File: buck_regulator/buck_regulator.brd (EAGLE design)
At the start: 69.5 x 52.1 mm, 12 parts

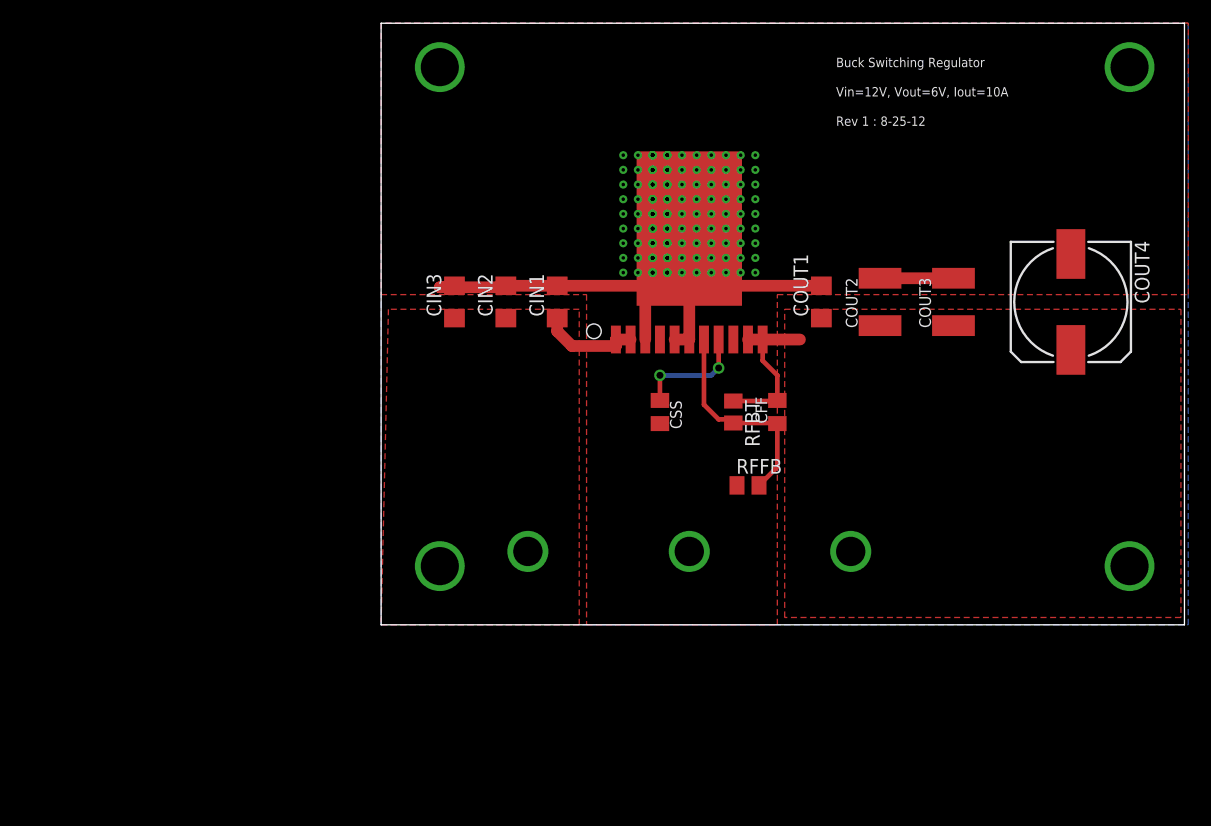
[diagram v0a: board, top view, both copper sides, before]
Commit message: buck_regulator: re-route for revision B
Change-Id: Ie95bbfd6e64e4db471db740f6a7ad1b08f6b97fa
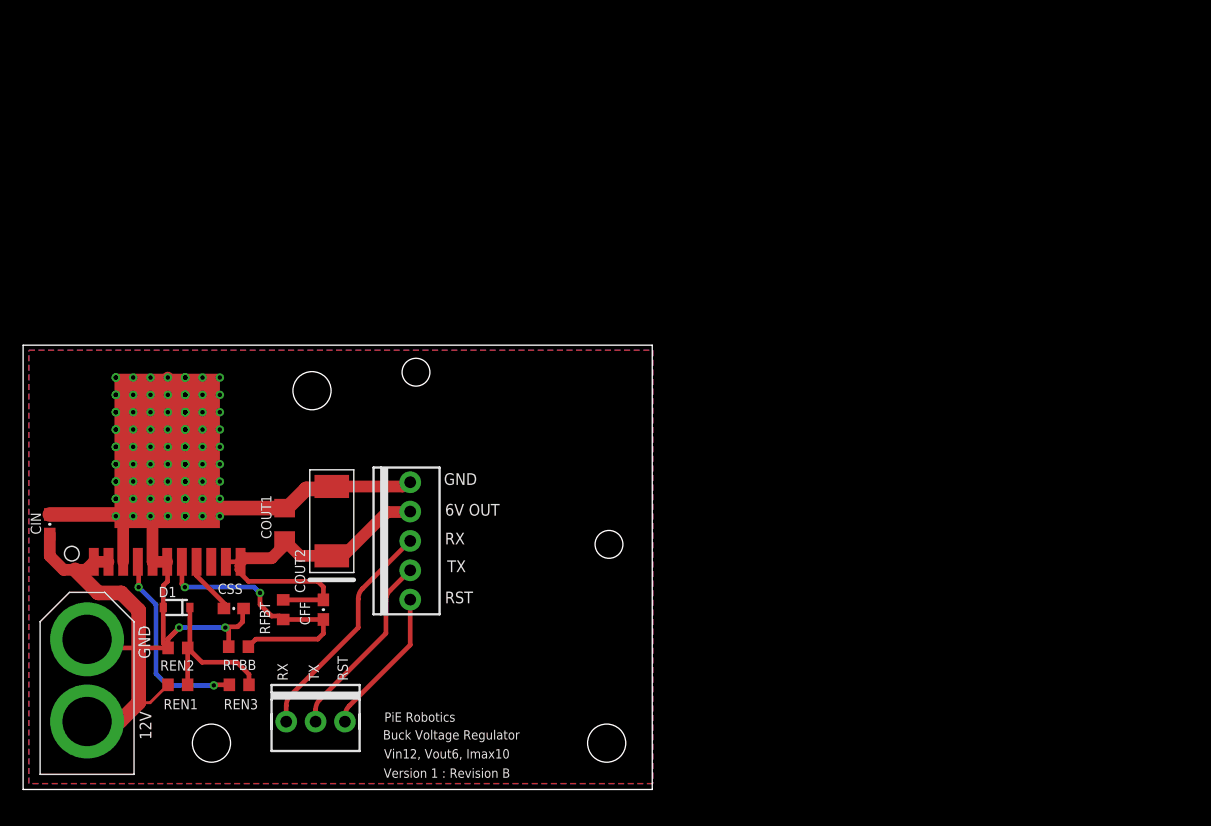
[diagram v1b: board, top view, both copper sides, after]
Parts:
- removed CIN1, CIN2, CIN3: (no value), resistor:C1206
- removed COUT3: (no value), resistor:C1812K
- removed COUT4: (no value), resistor:153CLV-1014
- removed RFFB: 2.37k, resistor:M0805
- added CIN: 10uF, pie:0603-CAP
- added D1: 5.1V, SparkFun:SOD-323
- added JP1: (no value), pie:1X03
- added REN1: 60k, pie:R0603
- added REN2: 30k, pie:R0603
- added REN3: 100, pie:R0603
- added RFBB: 2.37k, pie:R0603
- added U$2: XT60CONNECTOR, pie:XT60CONNECTOR
- added U$3, U$4, U$5: (no value), SparkFun:STAND-OFF
- added U$6, U$7: (no value), stand_off_servoc:STAND_OFF_SERVOC
- added U$8: M05, pie:1X05-MTA
- CFF: device resistor:C0805K -> pie:0603-CAP
- COUT1: value (none) -> 47uF; device resistor:C1206 -> SparkFun:1206
- COUT2: value (none) -> 470uF; device resistor:C1812K -> TANT_CASE_E:TANT_CASE_E
- CSS: value .47u -> .47uF; device resistor:C0805K -> pie:0603-CAP
- RFBT: device resistor:M0805 -> pie:R0603
- moved COUT2 51.1 mm to (26.2, 24.2)
- moved COUT1 50.3 mm to (22.1, 23.9)
- moved U$1 49.1 mm to (12.0, 30.3)
- moved CFF 42.8 mm to (25.5, 16.6), turned to 270 degrees
- moved RFBT 42.5 mm to (22.0, 16.6), turned to 90 degrees
- moved CSS 40.6 mm to (17.7, 16.6), turned to 0 degrees
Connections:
- removed net EN: U$1.4
- new net N$1: REN3.2, U$1.4
- new net N$2: JP1.1, U$8.3
- new net N$3: D1.1, REN1.1, REN2.2, REN3.1
- new net N$4: JP1.2, U$8.2
- new net N$5: JP1.3, U$8.1
- net FB: now also CFF.2, RFBB.1, RFBT.1; no longer CFF.1, RFBT.2, RFFB.2
- net GND: now also CIN.2, COUT2.NEG, D1.2, REN2.1, RFBB.2, U$2.GND, U$8.5; no longer CIN1.2, CIN2.2, CIN3.2, COUT2.2, COUT3.2, COUT4.-, RFFB.1
- net VIN: now also CIN.1, REN1.2, U$2.12V; no longer CIN1.1, CIN2.1, CIN3.1
- net VOUT: now also CFF.1, COUT2.POS, RFBT.2, U$8.4; no longer CFF.2, COUT2.1, COUT3.1, COUT4.+, RFBT.1
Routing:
- net GND: track 43.5 -> 72.4 mm, vias 153 -> 91
- net VIN: track 8.57 -> 31.0 mm
- net N$2: track 0.00 -> 19.9 mm, vias 1 -> 0
- net VOUT: track 14.1 -> 32.6 mm
- net N$1: track 0.00 -> 17.1 mm, vias 1 -> 2
- net N$4: track 0.00 -> 16.3 mm, vias 1 -> 0
- net N$3: track 0.00 -> 13.9 mm
- net N$5: track 0.00 -> 12.8 mm, vias 1 -> 0
- net FB: track 18.7 -> 24.2 mm, vias 0 -> 2
- net SS: track 9.98 -> 5.12 mm, vias 2 -> 0
- added copper zone on layer 1, net N$21
- removed copper zone on layer 1, net GND
- removed copper zone on layer 1, net VIN
- removed copper zone on layer 1, net VOUT
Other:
- board size 69.5 x 52.1 mm -> 54.4 x 38.4 mm
- board text added: "12V"
- board text added: "6V OUT"
- board text added: "Buck Voltage Regulator"
- board text added: "GND"
- board text added: "PiE Robotics"
- board text added: "RST"
- board text added: "RX"
- board text added: "TX"
- board text added: "Version 1 : Revision B"
- board text added: "Vin12, Vout6, Imax10"
- board text removed: "Buck Switching Regulator"
- board text removed: "Rev 1 : 8-25-12"
- board text removed: "Vin=12V, Vout=6V, Iout=10A"

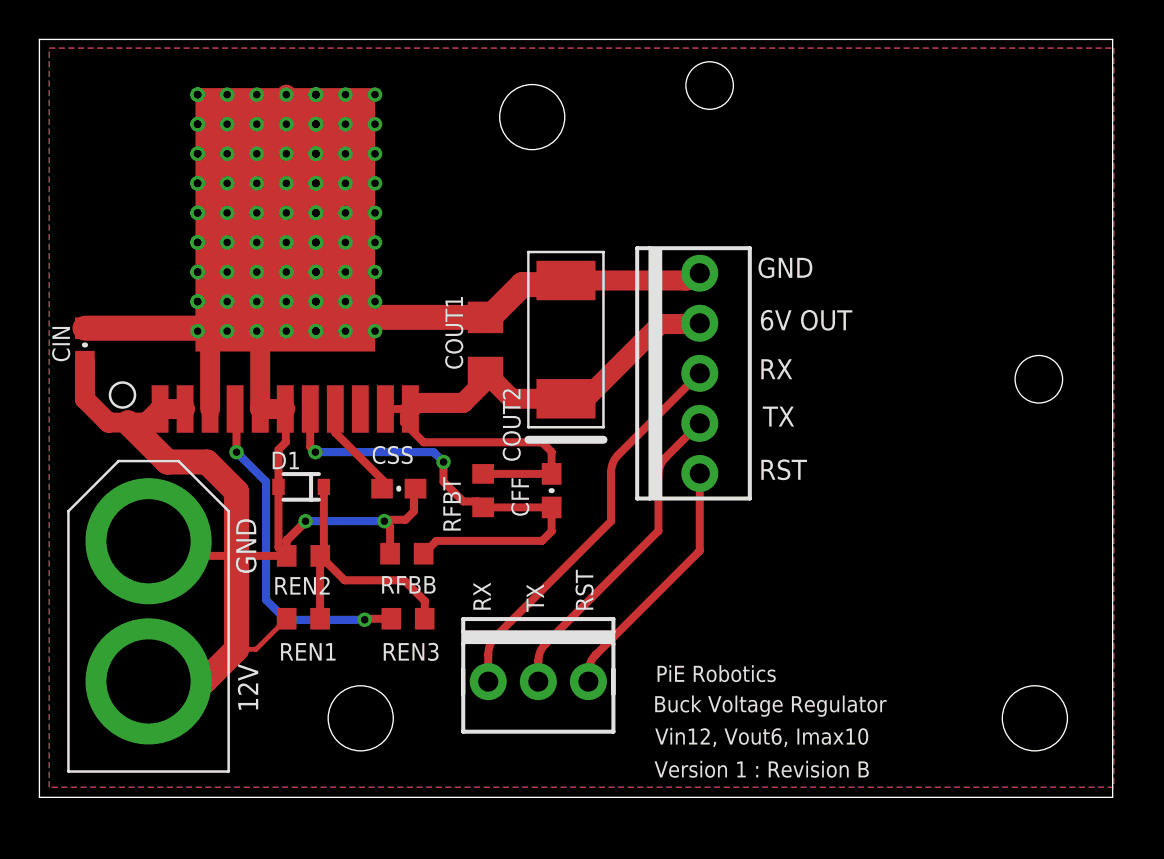
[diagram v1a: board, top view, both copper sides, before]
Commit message: Fix all boards to be at origin, fix dimension width to be 10 mil
Change-Id: I08bc507f450d0f63cfcc98eecb1f52bd6fb958a5
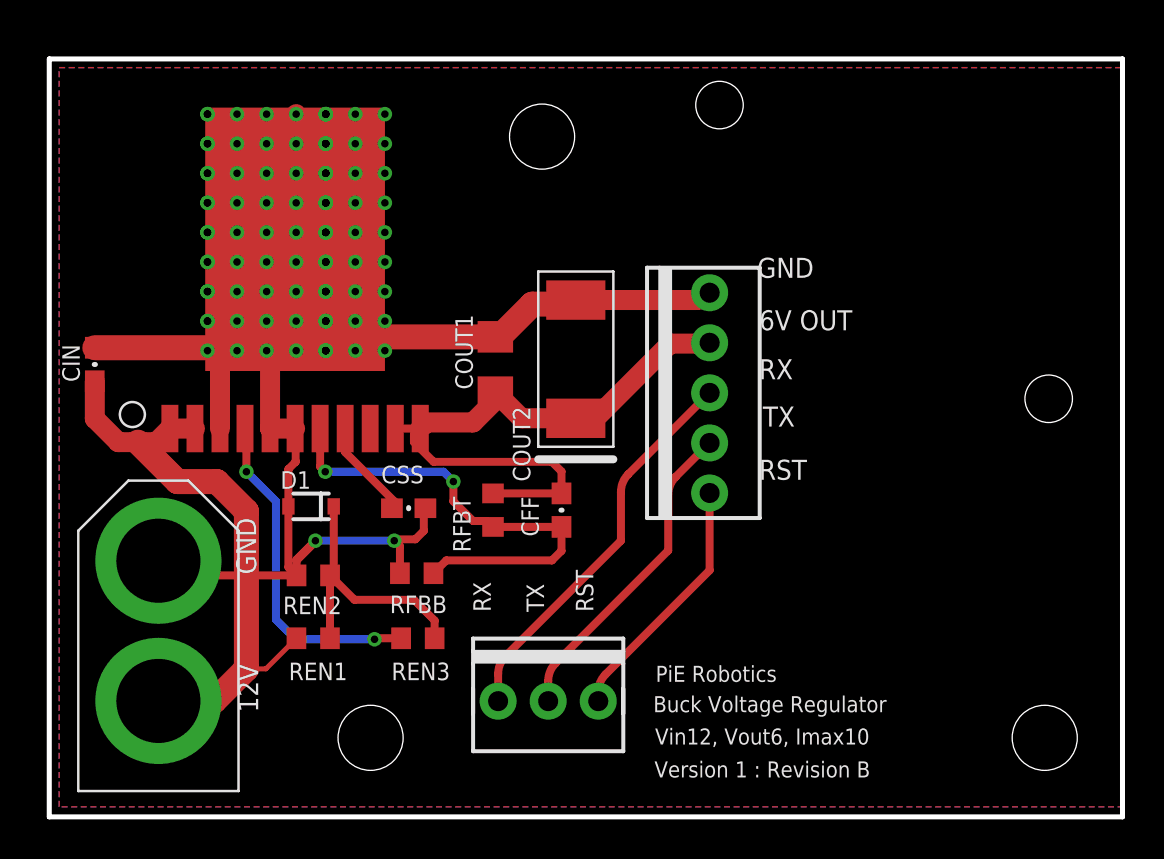
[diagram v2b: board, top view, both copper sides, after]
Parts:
- moved CIN 1.11 mm to (2.31, 22.9)
- moved COUT1 1.11 mm to (22.6, 22.9)
- moved COUT2 1.11 mm to (26.7, 23.2)
- moved U$4 1.11 mm to (25.0, 34.5)
- moved U$7 1.11 mm to (34.0, 36.1)
- moved CFF 1.11 mm to (26.0, 15.6)
- moved JP1 1.11 mm to (22.8, 5.87)
- moved REN1 1.11 mm to (13.4, 9.06)
- moved REN2 1.11 mm to (13.4, 12.2)
- moved REN3 1.11 mm to (18.7, 9.06)
- moved RFBB 1.11 mm to (18.6, 12.4)
- moved RFBT 1.11 mm to (22.5, 15.6)
- moved U$3 1.11 mm to (50.5, 4.01)
- moved U$5 1.11 mm to (16.3, 4.01)
- moved U$2 1.11 mm to (9.60, 1.31)
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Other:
- board size 54.4 x 38.4 mm -> 54.4 x 38.5 mm
